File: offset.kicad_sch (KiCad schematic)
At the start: 34 parts, among them U11 OPA2189DGK, U12 TMUX1108PW, U18 TMUX6219DGK, U19 TCA0372

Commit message: Everything assigned except for wierd shit.
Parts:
- added C116: 0u1, Capacitor_SMD:C_0402_1005Metric, symbol Device:C
- U18: value TMUX6219DGK -> DG419D; footprint Package_SO:VSSOP-8_3x3mm_P0.65mm -> Package_SO:SOIC-8_3.9x4.9mm_P1.27mm; symbol Parts:TMUX6219DGK -> Parts:DG419; now left out of the parts list
- renumbered C106 to C114, C107 to C115
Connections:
- net GNDPWR: now also C116.2
- net +2V5 renamed +3V3A
- net +3V3A: now also C116.1
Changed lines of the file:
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@@
 	)
 	(junction
+		(at 104.14 135.89)
+		(diameter 0)
+		(color 0 0 0 0)
+	)
+	(junction
 		(at 133.35 90.17)
 		(diameter 0)
@@
 		(on_board yes)
 		(dnp no)
-		(property "Reference" "C106"
+		(property "Reference" "C114"
 			(at 82.55 99.822 0)
 			(effects
@@
 			(project "lincal"
 				(path "/b054cef4-39e3-49d8-aff0-7ba5a206c187/fd210975-34eb-456f-9075-cf344b0a559b"
-					(reference "C106")
+					(reference "C114")
 					(unit 1)
 				)
@@
 		(on_board yes)
 		(dnp no)
-		(property "Reference" "C107"
+		(property "Reference" "C115"
 			(at 82.55 107.442 0)
 			(effects
@@
 			(project "lincal"
 				(path "/b054cef4-39e3-49d8-aff0-7ba5a206c187/fd210975-34eb-456f-9075-cf344b0a559b"
-					(reference "C107")
+					(reference "C115")
 					(unit 1)
 				)
@@
 	)
 	(symbol
+		(lib_id "power:GNDPWR")
+		(at 104.14 143.51 0)
+		(mirror y)
+		(unit 1)
+		(exclude_from_sim no)
+		(in_bom yes)
+		(on_board yes)
+		(dnp no)
+		(property "Reference" "#PWR0367"
+			(at 104.14 149.86 0)
+			(effects
+				(font
+					(size 1.27 1.27)
+				)
+				(hide yes)
+			)
+		)
+		(property "Value" "GNDPWR"
+			(at 104.14 146.812 0)
+			(effects
+				(font
+					(size 1.27 1.27)
+				)
+				(hide yes)
+			)
+		)
+		(property "Footprint" ""
+			(at 104.14 144.78 0)
+			(effects
+				(font
+					(size 1.27 1.27)
+				)
+				(hide yes)
+			)
+		)
+		(property "Datasheet" ""
+			(at 104.14 144.78 0)
+			(effects
+				(font
+					(size 1.27 1.27)
+				)
+				(hide yes)
+			)
+		)
+		(property "Description" "Power symbol creates a global label with name \"GNDPWR\" , global ground"
+			(at 104.14 143.51 0)
+			(effects
+				(font
+					(size 1.27 1.27)
+				)
+				(hide yes)
+			)
+		)
+		(pin "1"
+		)
+		(instances
+			(project "lincal"
+				(path "/b054cef4-39e3-49d8-aff0-7ba5a206c187/fd210975-34eb-456f-9075-cf344b0a559b"
+					(reference "#PWR0367")
+					(unit 1)
+				)
+			)
+		)
+	)
+	(symbol
 		(lib_id "Parts:+18V")
 		(at 93.98 120.65 0)
@@
 	)
 	(symbol
-		(lib_id "Parts:TMUX6219DGK")
+		(lib_id "Parts:DG419")
 		(at 93.98 129.54 0)
 		(mirror y)
 		(unit 1)
 		(exclude_from_sim no)
-		(in_bom yes)
+		(in_bom no)
 		(on_board yes)
 		(dnp no)
@@
 			)
 		)
-		(property "Value" "TMUX6219DGK"
+		(property "Value" "DG419D"
 			(at 102.362 122.174 0)
 			(effects
@@
 			)
 		)
-		(property "Footprint" "Package_SO:VSSOP-8_3x3mm_P0.65mm"
+		(property "Footprint" "Package_SO:SOIC-8_3.9x4.9mm_P1.27mm"
 			(at 93.98 129.54 0)
 			(effects
@@
 			)
 		)
-		(property "Datasheet" "https://www.ti.com/lit/gpn/tmux6219"
+		(property "Datasheet" "https://www.ti.com/lit/gpn/tmux7219"
 			(at 93.98 129.54 0)
 			(effects
@@
 	)
 	(symbol
+		(lib_id "Parts:+3V3A")
+		(at 104.14 135.89 0)
+		(unit 1)
+		(exclude_from_sim no)
+		(in_bom yes)
+		(on_board yes)
+		(dnp no)
+		(property "Reference" "#PWR0364"
+			(at 104.14 139.7 0)
+			(effects
+				(font
+					(size 1.27 1.27)
+				)
+				(hide yes)
+			)
+		)
+		(property "Value" "+3V3A"
+			(at 107.95 134.62 0)
+			(do_not_autoplace yes)
+			(effects
+				(font
+					(size 1.27 1.27)
+				)
+			)
+		)
+		(property "Footprint" ""
+			(at 104.14 135.89 0)
+			(effects
+				(font
+					(size 1.27 1.27)
+				)
+				(hide yes)
+			)
+		)
+		(property "Datasheet" ""
+			(at 104.14 135.89 0)
+			(effects
+				(font
+					(size 1.27 1.27)
+				)
+				(hide yes)
+			)
+		)
+		(property "Description" "Power symbol creates a global label with name {dblquote}+3V3A{dblquote}"
+			(at 104.14 135.89 0)
+			(effects
+				(font
+					(size 1.27 1.27)
+				)
+				(hide yes)
+			)
+		)
+		(pin "1"
+		)
+		(instances
+			(project "lincal"
+				(path "/b054cef4-39e3-49d8-aff0-7ba5a206c187/fd210975-34eb-456f-9075-cf344b0a559b"
+					(reference "#PWR0364")
+					(unit 1)
+				)
+			)
+		)
+	)
+	(symbol
 		(lib_id "power:GNDPWR")
 		(at 82.55 85.09 0)
@@
 	)
 	(symbol
+		(lib_id "Device:C")
+		(at 104.14 139.7 0)
+		(unit 1)
+		(exclude_from_sim no)
+		(in_bom yes)
+		(on_board yes)
+		(dnp no)
+		(property "Reference" "C116"
+			(at 104.14 137.922 0)
+			(effects
+				(font
+					(size 1.27 1.27)
+				)
+				(justify left)
+			)
+		)
+		(property "Value" "0u1"
+			(at 104.14 140.97 0)
+			(effects
+				(font
+					(size 1.27 1.27)
+				)
+				(justify left top)
+			)
+		)
+		(property "Footprint" "Capacitor_SMD:C_0402_1005Metric"
+			(at 105.1052 143.51 0)
+			(effects
+				(font
+					(size 1.27 1.27)
+				)
+				(hide yes)
+			)
+		)
+		(property "Datasheet" "50V"
+			(at 104.14 139.7 0)
+			(effects
+				(font
+					(size 1.27 1.27)
+				)
+				(hide yes)
+			)
+		)
+		(property "Description" "Unpolarized capacitor"
+			(at 104.14 139.7 0)
+			(effects
+				(font
+					(size 1.27 1.27)
+				)
+				(hide yes)
+			)
+		)
+		(property "LCSC" "C307331"
+			(at 104.14 139.7 0)
+			(effects
+				(font
+					(size 1.27 1.27)
+				)
+				(hide yes)
+			)
+		)
+		(pin "2"
+		)
+		(pin "1"
+		)
+		(instances
+			(project "lincal"
+				(path "/b054cef4-39e3-49d8-aff0-7ba5a206c187/fd210975-34eb-456f-9075-cf344b0a559b"
+					(reference "C116")
+					(unit 1)
+				)
+			)
+		)
+	)
+	(symbol
 		(lib_id "power:PWR_FLAG")
 		(at 194.31 127 0)
@@
 					(unit 1)
 				)
-			)
-		)
-	)
-	(symbol
-		(lib_id "power:+2V5")
-		(at 104.14 135.89 0)
-		(unit 1)
-		(exclude_from_sim no)
-		(in_bom yes)
-		(on_board yes)
-		(dnp no)
-		(property "Reference" "#PWR0219"
-			(at 104.14 139.7 0)
-			(effects
-				(font
-					(size 1.27 1.27)
-				)
-				(hide yes)
-			)
-		)
-		(property "Value" "+2V5"
-			(at 107.696 134.366 0)
-			(effects
-				(font
-					(size 1.27 1.27)
-				)
-			)
-		)
-		(property "Footprint" ""
-			(at 104.14 135.89 0)
-			(effects
-				(font
-					(size 1.27 1.27)
-				)
-				(hide yes)
-			)
-		)
-		(property "Datasheet" ""
-			(at 104.14 135.89 0)
-			(effects
-				(font
-					(size 1.27 1.27)
-				)
-				(hide yes)
-			)
-		)
-		(property "Description" "Power symbol creates a global label with name \"+2V5\""
-			(at 104.14 135.89 0)
-			(effects
-				(font
-					(size 1.27 1.27)
-				)
-				(hide yes)
-			)
-		)
-		(pin "1"
-		)
-		(instances
-			(project "lincal"
-				(path "/b054cef4-39e3-49d8-aff0-7ba5a206c187/fd210975-34eb-456f-9075-cf344b0a559b"
-					(reference "#PWR0219")
-					(unit 1)
-				)

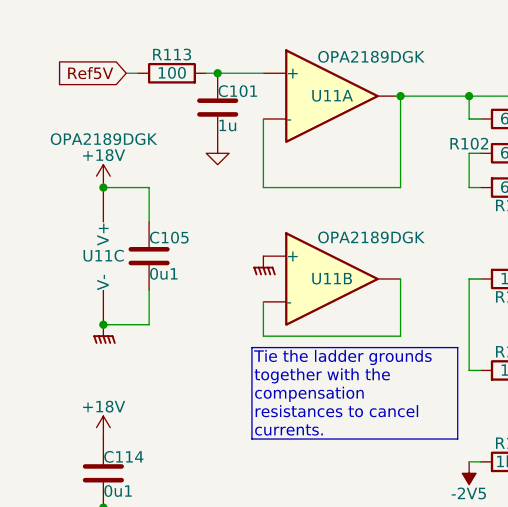
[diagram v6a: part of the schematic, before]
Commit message: Layout underway
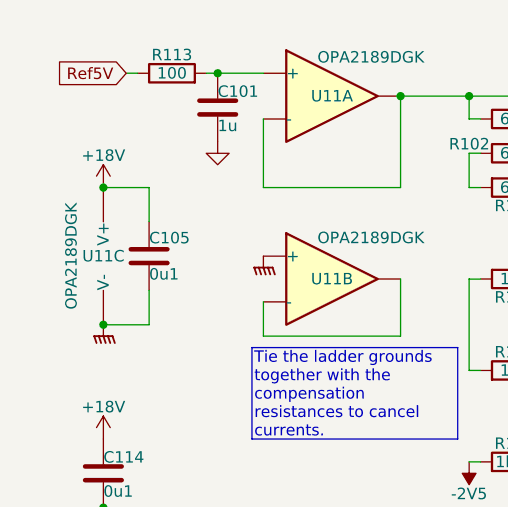
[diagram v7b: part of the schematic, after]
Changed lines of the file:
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@@
 		)
 		(property "Value" "OPA2189DGK"
-			(at 82.55 64.516 0)
+			(at 78.994 77.47 90)
 			(effects
 				(font

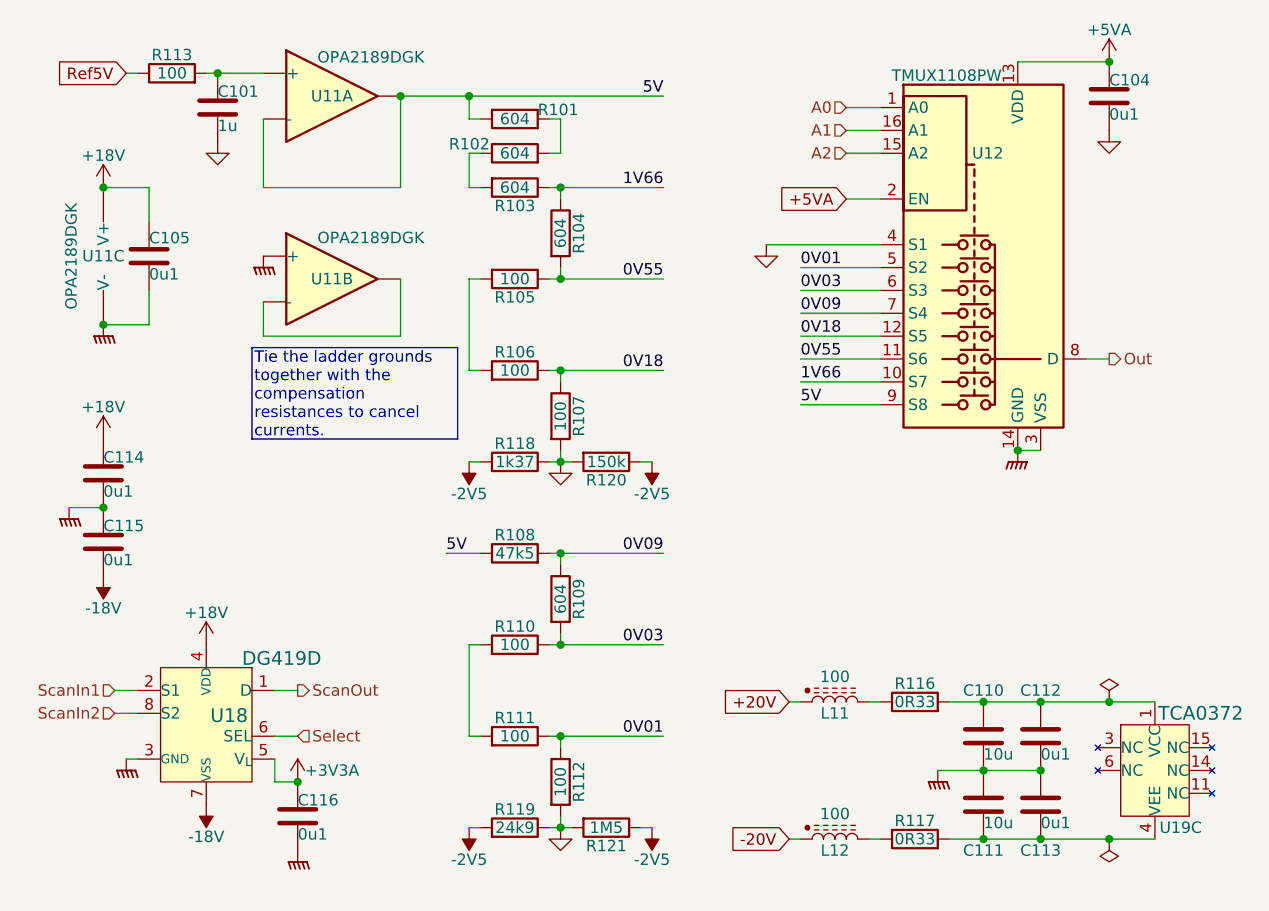
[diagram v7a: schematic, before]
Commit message: Whew.  DACs routed
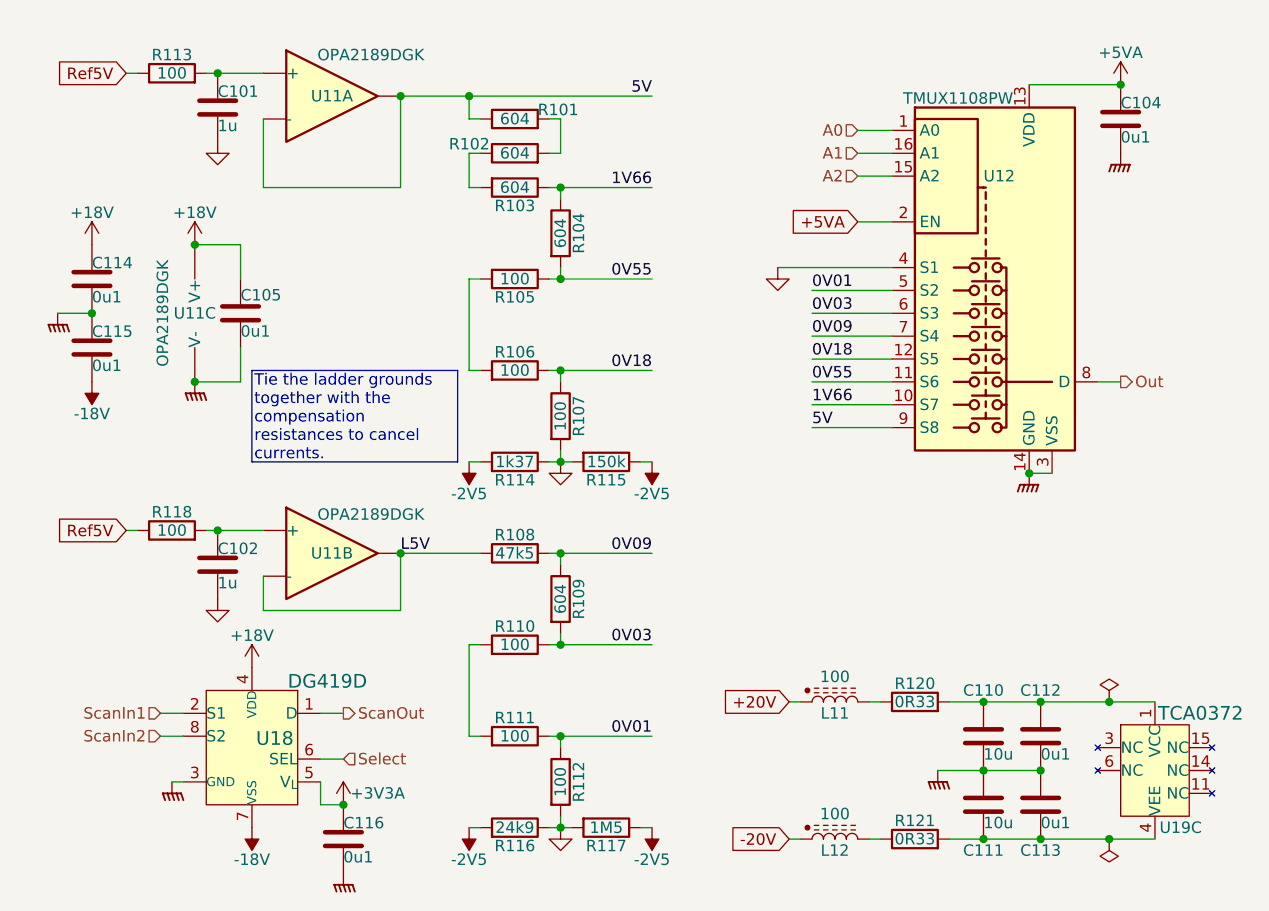
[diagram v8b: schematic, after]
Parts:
- added C102: 1u, Capacitor_SMD:C_0402_1005Metric, symbol Device:C
- added R118: 100, Resistor_SMD:R_0402_1005Metric, symbol Device:R
- U11: footprint Package_SO:MSOP-8_3x3mm_P0.65mm -> Parts:OPA2189
- renumbered R118 to R114, R120 to R115, R119 to R116, R121 to R117, R116 to R120, R117 to R121
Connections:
- net 5V: now also U11.1, U11.2 (-); no longer R108.1, U11.1, U11.2 (-)
- net GND: now also C102.2; no longer C104.2
- net GNDPWR: now also C104.2; no longer U11.5 (+)
- net Ref5V: now also R118.1
- net at C101.1, R113.2: now also U11.3 (+); no longer U11.3 (+)
- new net: C102.1, R118.2, U11.5 (+)
- new net L5V: R108.1, U11.6 (-), U11.7
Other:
- moved on the sheet: C104, C105, C114, C115, C116, U11A, U11B, U11C, U12, U18
